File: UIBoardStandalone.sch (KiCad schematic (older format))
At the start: 61 parts, among them J1 Conn_02x08_Odd_Even, J2 Conn_02x15_Odd_Even, SW1 Button_X, SW10 Button_6, SW11 Button_S, SW12 Button_7, SW13 Button_8, SW14 Button_9, SW15 Button_G, SW16 Button_Y, SW17 Button_0, SW18 Button_Z, SW2 Button_R, SW3 Button_1, SW4 Button_2, SW5 Button_3, SW6 Button_P, SW7 Button_M, SW8 Button_4, SW9 Button_5, U1 HD1077R, U10 HD1077R, U11 HD1077R, U12 HD1077R, U13 HD1077R, U14 HD1077R, U15 HD1077R, U16 HD1077R, U17 MM74C923WM, U2 HD1077R, U3 HD1077R, U4 HD1077R, U5 HD1077R, U6 HD1077R, U7 HD1077R, U8 HD1077R, U9 HD1077R

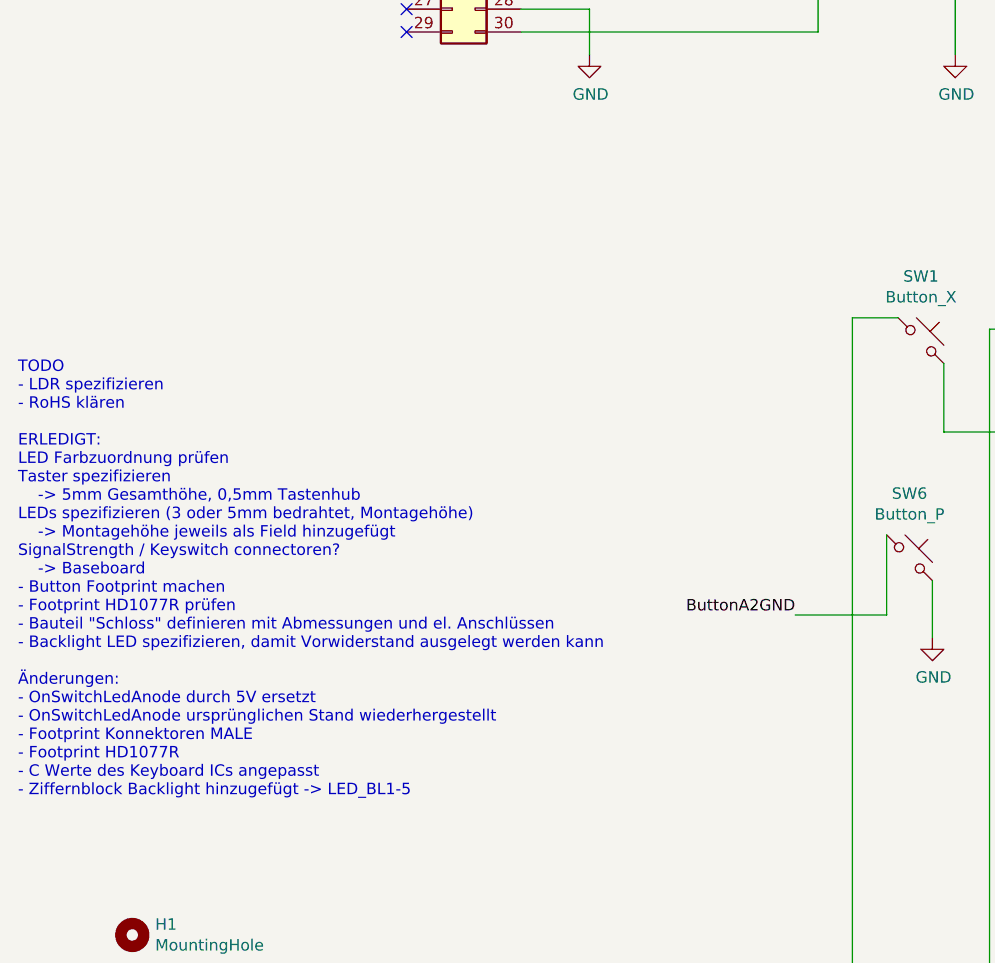
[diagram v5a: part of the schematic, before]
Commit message: - SW1 entfernt
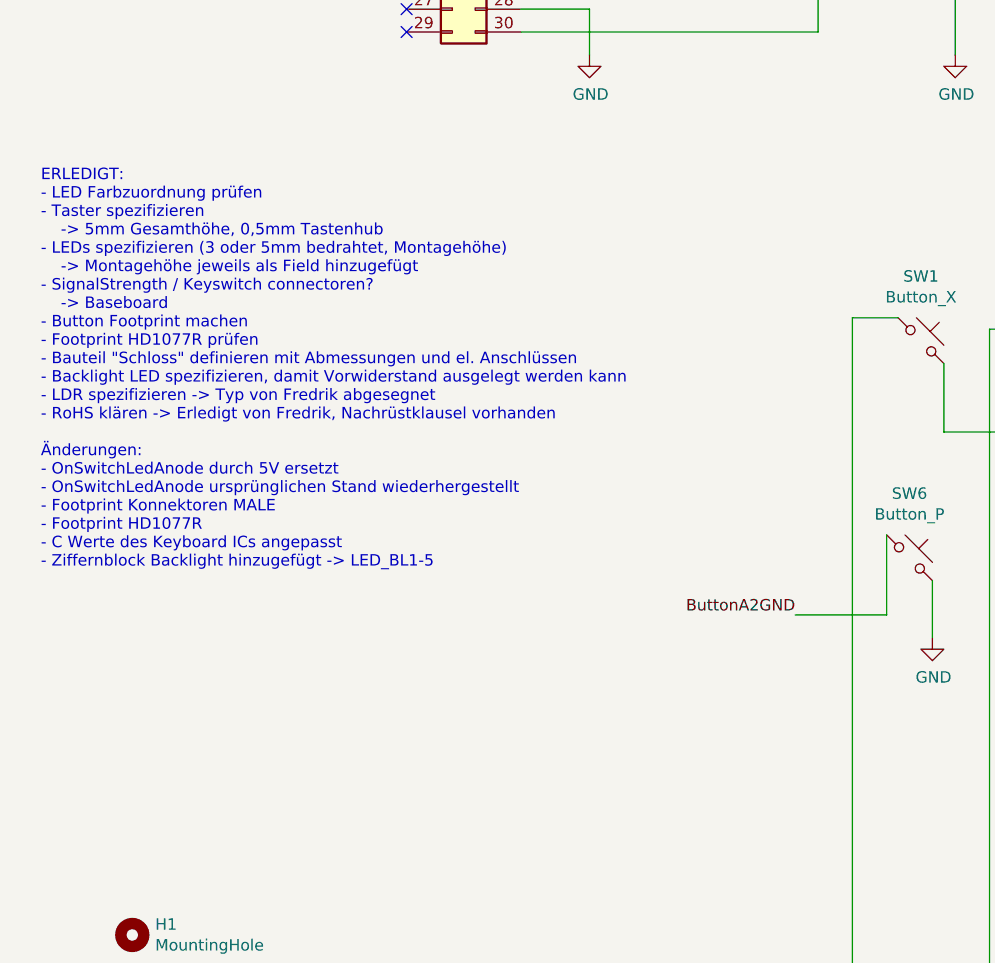
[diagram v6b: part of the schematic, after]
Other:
- note added: "ERLEDIGT:\n- LED Farbzuordnung prüfen\n- Taster spezifizieren\n -> 5mm Gesamthöhe, 0,5mm Tastenhub\n- LEDs spezifizieren (3 oder 5mm bedrahtet, Montagehöhe)\n -> Montagehöhe jeweils als Field hinzugefügt\n- SignalStrength / Keyswitch connectoren?\n -> Baseboard\n- Button Footprint machen\n- Footprint HD1077R prüfen\n- Bauteil "Schloss" definieren mit Abmessungen und el. Anschlüssen\n- Backlight L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"
- note removed: "TODO\n- LDR spezifizieren\n- RoHS klären\n\nERLEDIGT:\nLED Farbzuordnung prüfen\nTaster spezifizieren\n -> 5mm Gesamthöhe, 0,5mm Tastenhub\nLEDs spezifizieren (3 oder 5mm bedrahtet, Montagehöhe)\n -> Montagehöhe jeweils als Field hinzugefügt\nSignalStrength / Keyswitch connectoren?\n -> Baseboard\n- Button Footprint machen\n- Footprint HD1077R prüfen\n- Bauteil "Schloss" definieren mit Abmessunge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"
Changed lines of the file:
@@
 Text Label 9450 4550 2    50   ~ 0
 LED_GN
-Text Notes 1050 8550 0    50   ~ 0
-TODO\n- LDR spezifizieren\n- RoHS klären\n\nERLEDIGT:\nLED Farbzuordnung prüfen\nTaster spezifizieren\n    -> 5mm Gesamthöhe, 0,5mm Tastenhub\nLEDs spezifizieren (3 oder 5mm bedrahtet, Montagehöhe)\n    -> Montagehöhe jeweils als Field hinzugefügt\nSignalStrength / Keyswitch connectoren?\n    -> Baseboard\n- Button Footprint machen\n- Footprint HD1077R prüfen\n- Bauteil "Schloss" definieren mit Abmessungen und el. Anschlüssen\n- Backlight LED spezifizieren, damit Vorwiderstand ausgelegt werden kann\n\nÄnderungen:\n- OnSwitchLedAnode durch 5V ersetzt\n- OnSwitchLedAnode ursprünglichen Stand wiederhergestellt\n- Footprint Konnektoren MALE\n- Footprint HD1077R\n- C Werte des Keyboard ICs angepasst\n- Ziffernblock Backlight hinzugefügt -> LED_BL1-5
+Text Notes 1150 7550 0    50   ~ 0
+ERLEDIGT:\n- LED Farbzuordnung prüfen\n- Taster spezifizieren\n    -> 5mm Gesamthöhe, 0,5mm Tastenhub\n- LEDs spezifizieren (3 oder 5mm bedrahtet, Montagehöhe)\n    -> Montagehöhe jeweils als Field hinzugefügt\n- SignalStrength / Keyswitch connectoren?\n    -> Baseboard\n- Button Footprint machen\n- Footprint HD1077R prüfen\n- Bauteil "Schloss" definieren mit Abmessungen und el. Anschlüssen\n- Backlight LED spezifizieren, damit Vorwiderstand ausgelegt werden kann\n- LDR spezifizieren -> Typ von Fredrik abgesegnet\n- RoHS klären -> Erledigt von Fredrik, Nachrüstklausel vorhanden\n\nÄnderungen:\n- OnSwitchLedAnode durch 5V ersetzt\n- OnSwitchLedAnode ursprünglichen Stand wiederhergestellt\n- Footprint Konnektoren MALE\n- Footprint HD1077R\n- C Werte des Keyboard ICs angepasst\n- Ziffernblock Backlight hinzugefügt -> LED_BL1-5
 Wire Wire Line
 	13650 4700 13900 4700

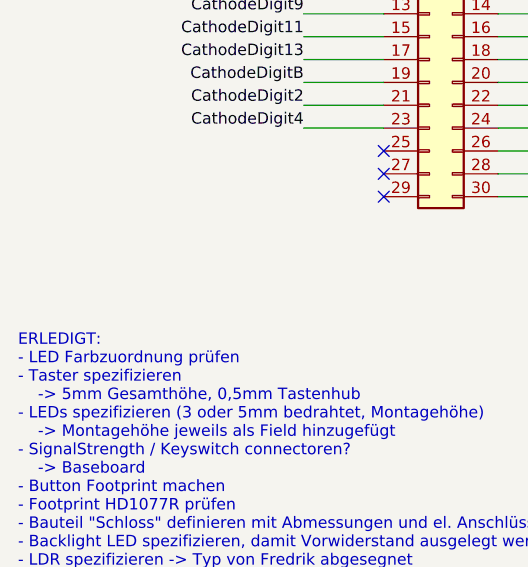
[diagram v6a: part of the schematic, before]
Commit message: - Wert und Footprint der LED Vorwiderstaende angepasst
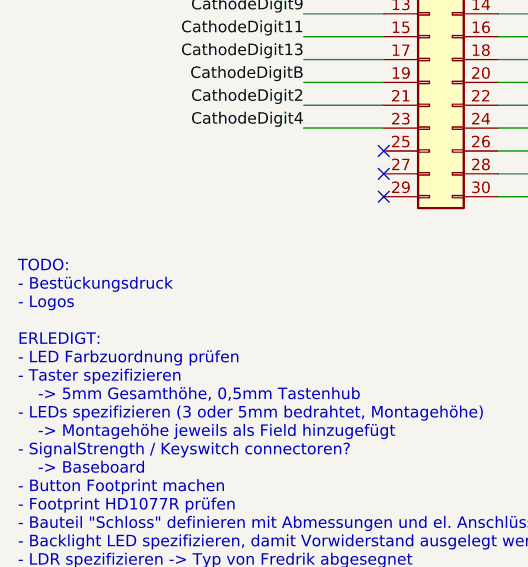
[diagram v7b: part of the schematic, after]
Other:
- note added: "TODO:\n- Bestückungsdruck\n- Logos\n\nERLEDIGT:\n- LED Farbzuordnung prüfen\n- Taster spezifizieren\n -> 5mm Gesamthöhe, 0,5mm Tastenhub\n- LEDs spezifizieren (3 oder 5mm bedrahtet, Montagehöhe)\n -> Montagehöhe jeweils als Field hinzugefügt\n- SignalStrength / Keyswitch connectoren?\n -> Baseboard\n- Button Footprint machen\n- Footprint HD1077R prüfen\n- Bauteil "Schloss" definieren mit Abmessun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"
- note removed: "ERLEDIGT:\n- LED Farbzuordnung prüfen\n- Taster spezifizieren\n -> 5mm Gesamthöhe, 0,5mm Tastenhub\n- LEDs spezifizieren (3 oder 5mm bedrahtet, Montagehöhe)\n -> Montagehöhe jeweils als Field hinzugefügt\n- SignalStrength / Keyswitch connectoren?\n -> Baseboard\n- Button Footprint machen\n- Footprint HD1077R prüfen\n- Bauteil "Schloss" definieren mit Abmessungen und el. Anschlüssen\n- Backlight L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"
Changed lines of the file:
@@
 LED_GN
 Text Notes 1150 7550 0    50   ~ 0
-ERLEDIGT:\n- LED Farbzuordnung prüfen\n- Taster spezifizieren\n    -> 5mm Gesamthöhe, 0,5mm Tastenhub\n- LEDs spezifizieren (3 oder 5mm bedrahtet, Montagehöhe)\n    -> Montagehöhe jeweils als Field hinzugefügt\n- SignalStrength / Keyswitch connectoren?\n    -> Baseboard\n- Button Footprint machen\n- Footprint HD1077R prüfen\n- Bauteil "Schloss" definieren mit Abmessungen und el. Anschlüssen\n- Backlight LED spezifizieren, damit Vorwiderstand ausgelegt werden kann\n- LDR spezifizieren -> Typ von Fredrik abgesegnet\n- RoHS klären -> Erledigt von Fredrik, Nachrüstklausel vorhanden\n\nÄnderungen:\n- OnSwitchLedAnode durch 5V ersetzt\n- OnSwitchLedAnode ursprünglichen Stand wiederhergestellt\n- Footprint Konnektoren MALE\n- Footprint HD1077R\n- C Werte des Keyboard ICs angepasst\n- Ziffernblock Backlight hinzugefügt -> LED_BL1-5
+TODO:\n- Bestückungsdruck\n- Logos\n\nERLEDIGT:\n- LED Farbzuordnung prüfen\n- Taster spezifizieren\n    -> 5mm Gesamthöhe, 0,5mm Tastenhub\n- LEDs spezifizieren (3 oder 5mm bedrahtet, Montagehöhe)\n    -> Montagehöhe jeweils als Field hinzugefügt\n- SignalStrength / Keyswitch connectoren?\n    -> Baseboard\n- Button Footprint machen\n- Footprint HD1077R prüfen\n- Bauteil "Schloss" definieren mit Abmessungen und el. Anschlüssen\n- Backlight LED spezifizieren, damit Vorwiderstand ausgelegt werden kann\n- LDR spezifizieren -> Typ von Fredrik abgesegnet\n- RoHS klären -> Erledigt von Fredrik, Nachrüstklausel vorhanden\n\nÄnderungen:\n- OnSwitchLedAnode durch 5V ersetzt\n- OnSwitchLedAnode ursprünglichen Stand wiederhergestellt\n- Footprint Konnektoren MALE\n- Footprint HD1077R\n- C Werte des Keyboard ICs angepasst\n- Ziffernblock Backlight hinzugefügt -> LED_BL1-5
 Wire Wire Line
 	13650 4700 13900 4700
